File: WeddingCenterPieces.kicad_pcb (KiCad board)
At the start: 2 copper layers, 80 x 57 mm, 72 parts, among them J1 USB_C_Receptacle_USB2.0_16P, J2 DBG, J5 WS2812, K1 SW_Push, K2 SW_Push, K3 SW_Push, K4 SW_Push, SW1 Btn_OnBoard, SW2 RST, SW3 BOOT, U1 RP2040, U2 TPD2E2U06, U4 TXS0101DBV, U5 W25Q128JVSIQ, U6 TVS0500DRV, U7 AP2112K-3.3, U8 TXS0101DBV, Y1 12MHz

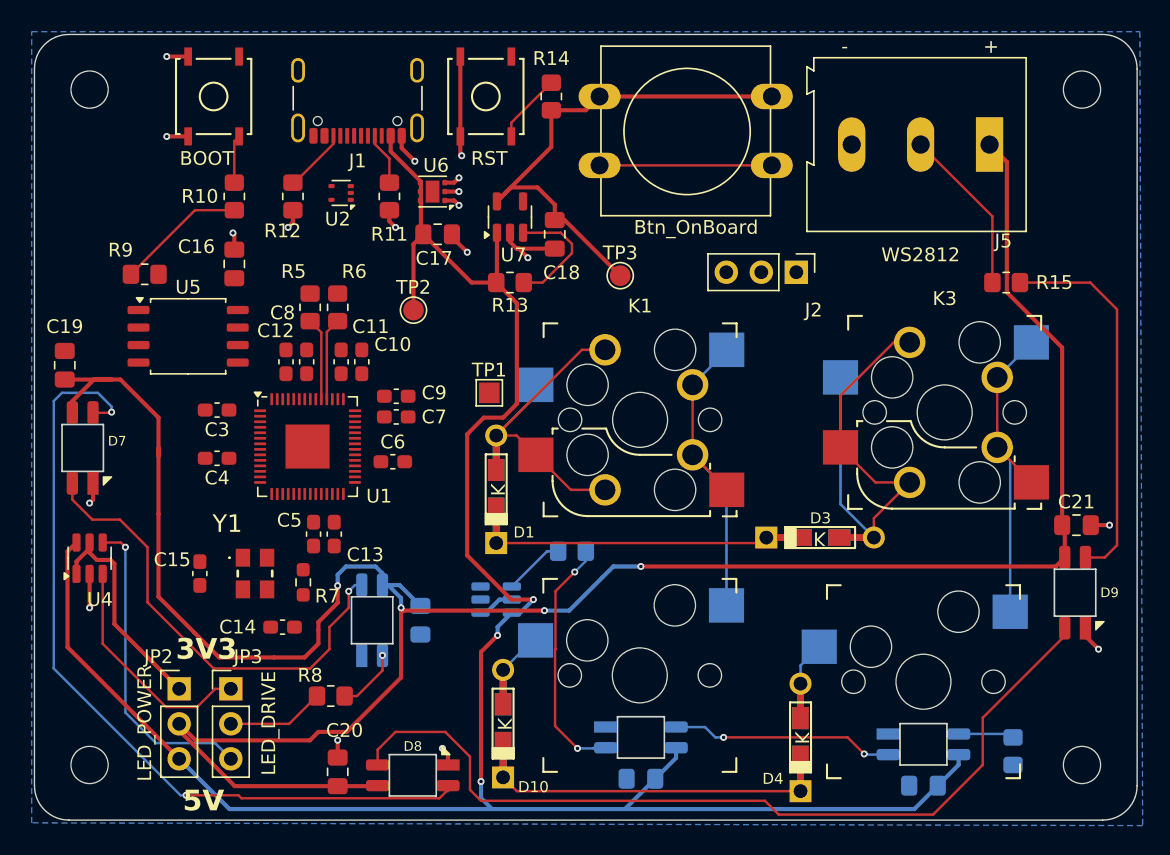
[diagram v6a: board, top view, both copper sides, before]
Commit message: Shrinking board to only have 2 key switches and a few other unnecessary components. Finished with routing the rest of the board.
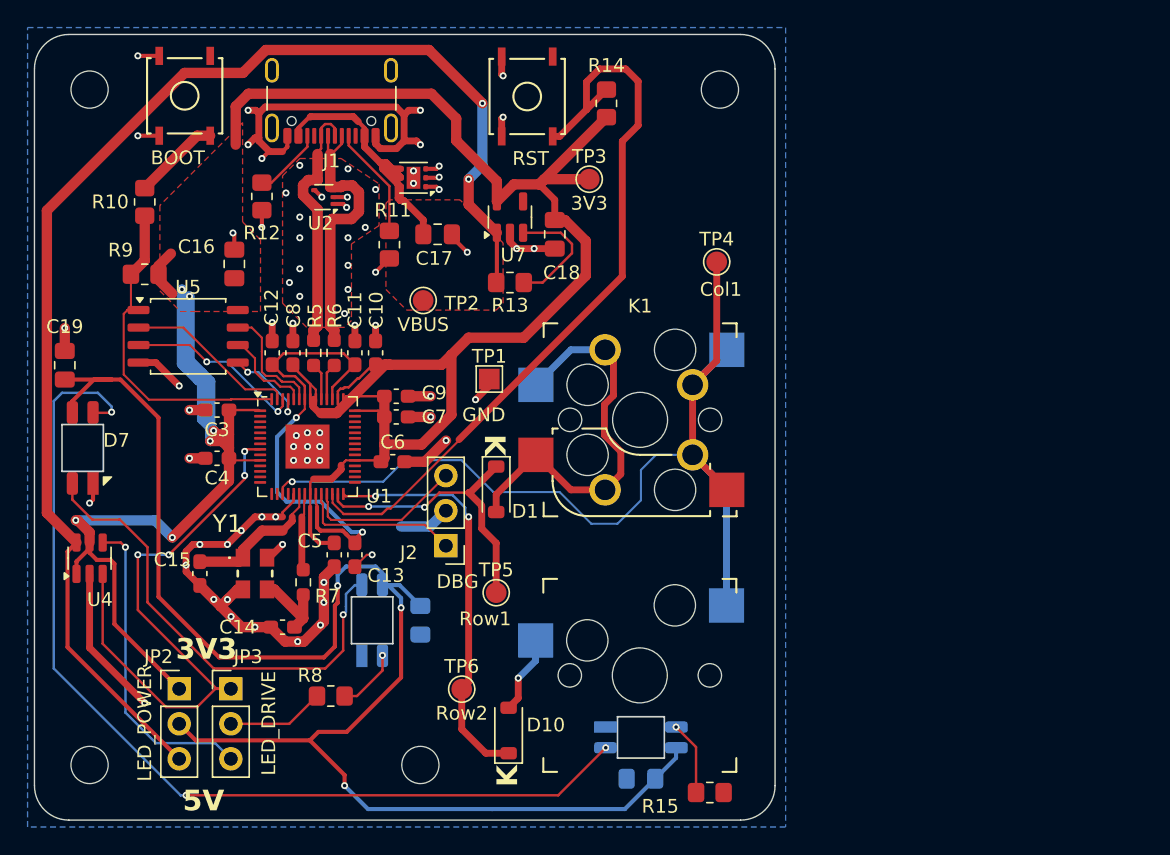
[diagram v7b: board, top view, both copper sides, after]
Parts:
- removed C20, C21, C23: 100nF, Capacitor_SMD:C_0805_2012Metric_Pad1.18x1.45mm_HandSolder
- removed D12, D8, D9: ~, Extra:SK6812-MINI-E_ReverseMount
- removed D3, D4: 1N4148W, Keebio-Parts:Diode-dual
- removed J5: WS2812, TerminalBlock:TerminalBlock_Altech_AK300-3_P5.00mm
- removed K3: SW_Push, keyswitches:Kailh_socket_MX_optional_reversible
- removed K4: SW_Push, keyswitches:Kailh_socket_MX
- removed R16, R17: 470, Resistor_SMD:R_0805_2012Metric_Pad1.20x1.40mm_HandSolder
- removed SW1: Btn_OnBoard, Button_Switch_THT:SW_PUSH-12mm
- removed U8: TXS0101DBV, Package_TO_SOT_SMD:SOT-23-6
- added TP4: Col1, TestPoint:TestPoint_Pad_D1.5mm, F.Cu at (135.5, 83.5)
- added TP5: Row1, TestPoint:TestPoint_Pad_D1.5mm, F.Cu at (119.5, 107.5)
- added TP6: Row2, TestPoint:TestPoint_Pad_D1.5mm, F.Cu at (117.0, 114.5)
- D1, D10: footprint Keebio-Parts:Diode-dual -> Diode_SMD:D_SOD-123
- R5, R6: footprint Resistor_SMD:R_0805_2012Metric_Pad1.20x1.40mm_HandSolder -> Resistor_SMD:R_0603_1608Metric_Pad0.98x0.95mm_HandSolder
- moved H4 48.0 mm to (114.0, 120.0)
- moved R15 42.8 mm to (135.0, 122.0), turned to 180 degrees
- moved J2 32.2 mm to (115.8, 104.1), turned to 180 degrees
- moved H2 26.3 mm to (135.7, 71.0)
- moved TP3 7.35 mm to (126.2, 77.5)
- moved R10 6.51 mm to (94.0, 79.2)
- moved R14 4.03 mm to (127.5, 72.0)
- moved R11 3.50 mm to (111.8, 82.2)
- moved R5 3.31 mm to (106.2, 90.1)
- moved R6 3.31 mm to (107.8, 90.1)
- moved SW2 3.00 mm to (121.8, 71.5)
- moved R12 2.25 mm to (102.5, 78.8)
- moved C13 2.12 mm to (109.2, 104.8)
- moved C5 2.12 mm to (107.8, 104.8)
- moved SW3 2.10 mm to (96.9, 71.5)
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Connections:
- C22 pad 1: VBUS -> /Lighting/PowerRail
- D11 pad 3: VBUS -> /Lighting/PowerRail
- D7 pad 4: Net-(D7-DOUT) -> Net-(D11-DIN)
- R15 pad 2: Net-(D9-DOUT) -> Net-(D11-DOUT)
- U1 pad 18: /Key Switches/COL_2 -> unconnected-(U1-GPIO15-Pad18)
- U1 pad 9: /Lighting/DIN_1 -> unconnected-(U1-GPIO7-Pad9)
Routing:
- net +3V3: track 56.6 -> 187.7 mm, vias 0 -> 6
- net GND: track 37.2 -> 122.6 mm, vias 18 -> 76
- net /Lighting/PowerRail: track 177.9 -> 111.3 mm, vias 4 -> 3
- net Net-(D8-DOUT): track 63.3 -> 0.00 mm
- net Net-(D7-DOUT): track 59.5 -> 0.00 mm, vias 2 -> 0
- net Net-(D11-DIN): track 18.0 -> 71.3 mm, vias 2 -> 3
- net Net-(U1-RUN): track 5.10 -> 55.6 mm
- net /Key Switches/COL_1: track 24.2 -> 70.1 mm, vias 0 -> 1
- net VBUS: track 156.0 -> 118.0 mm, vias 3 -> 2
- net /Microcontroller/+1.1V: track 0.00 -> 35.5 mm, vias 0 -> 2
- net Net-(D3-A): track 34.1 -> 0.00 mm
- net Net-(D9-DOUT): track 27.6 -> 0.00 mm
- net /Lighting/DIN_0: track 16.8 -> 43.2 mm, vias 0 -> 4
- net /Key Switches/COL_2: track 24.5 -> 0.00 mm
- net /External Connectors/D-: track 0.00 -> 20.4 mm
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- added copper zone on F.Cu, net +3V3
- added copper zone on F.Cu, net GND
- added copper zone on F.Cu, net VBUS
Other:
- board size 80 x 57 mm -> 53.7 x 57 mm
- board text added: "K"
- board text removed: "+"
- board text removed: "-"

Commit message: Outputs generated and prepared for ordering.
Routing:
- net /Key Switches/COL_1: track 70.1 -> 70.6 mm, vias 1 -> 2
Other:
- rule pad_to_mask_clearance: 0.0508 -> 0
- board text added: "v02 Wedding_Test Bare_RP2040 2024-12"
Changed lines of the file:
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@@
 			(dielectric_constraints no)
 		)
-		(pad_to_mask_clearance 0.0508)
+		(pad_to_mask_clearance 0)
 		(allow_soldermask_bridges_in_footprints no)
 		(pcbplotparams
@@
 			(plotinvisibletext no)
 			(sketchpadsonfab no)
-			(subtractmaskfromsilk no)
+			(subtractmaskfromsilk yes)
 			(outputformat 1)
 			(mirror no)
-			(drillshape 1)
+			(drillshape 0)
 			(scaleselection 1)
-			(outputdirectory "")
+			(outputdirectory "gerbers/")
 		)
 	)
@@
 		(tags "resistor handsolder")
 		(property "Reference" "R15"
-			(at 3.6 -1 0)
+			(at 3.8 -0.4 0)
 			(layer "F.SilkS")
 			(effects
@@
 		(layer "Edge.Cuts")
 	)
+	(gr_text "v02\nWedding_Test\nBare_RP2040\n2024-12"
+		(at 123.75 79.875 0)
+		(layer "B.Cu")
+		(effects
+			(font
+				(size 1.5 1.5)
+				(thickness 0.3)
+				(bold yes)
+			)
+			(justify right bottom mirror)
+		)
+	)
 	(gr_text "3V3"
 		(at 96.25 112.475 0)
@@
 	)
 	(via
-		(at 105.8 97.9)
+		(at 105.8 98.1)
 		(size 0.508)
 		(drill 0.254)
@@
 	)
 	(via
-		(at 105.8 95.9)
+		(at 105.8 95.7)
 		(size 0.508)
 		(drill 0.254)
@@
 	)
 	(via
-		(at 106.7 95.9)
+		(at 107 95.7)
 		(size 0.508)
 		(drill 0.254)
@@
 	)
 	(via
-		(at 104.8 96.9)
+		(at 104.7 96.9)
 		(size 0.508)
 		(drill 0.254)
@@
 	)
 	(via
-		(at 104.8 97.9)
+		(at 104.7 98.1)
 		(size 0.508)
 		(drill 0.254)
@@
 	)
 	(via
-		(at 106.7 97.9)
+		(at 107 98.1)
 		(size 0.508)
 		(drill 0.254)
@@
 	)
 	(via
-		(at 106.7 96.9)
+		(at 107 96.9)
 		(size 0.508)
 		(drill 0.254)
@@
 	)
 	(segment
-		(start 118.45 102.85)
-		(end 118.45 101.188943)
+		(start 119.5 107.5)
+		(end 119.5 103.9)
 		(width 0.5)
 		(layer "F.Cu")
@@
 	)
 	(segment
-		(start 119.5 107.5)
-		(end 119.5 103.9)
+		(start 119.5 103.9)
+		(end 118.45 102.85)
+		(width 0.5)
+		(layer "F.Cu")
+		(net 7)
+	)
+	(segment
+		(start 118.45 102.85)
+		(end 118.45 99.4)
 		(width 0.5)
 		(layer "F.Cu")
@@
 	)
 	(segment
-		(start 117.611057 100.238943)
-		(end 119.5 98.35)
-		(width 0.5)
+		(start 117.5 100.238943)
+		(end 117.611057 100.238943)
+		(width 0.18)
 		(layer "F.Cu")
 		(net 7)
 	)
 	(segment
-		(start 117.5 100.238943)
-		(end 117.611057 100.238943)
+		(start 118.45 99.4)
+		(end 119.5 98.35)
 		(width 0.5)
 		(layer "F.Cu")
@@
 	)
 	(segment
-		(start 119.5 103.9)
-		(end 118.45 102.85)
-		(width 0.5)
-		(layer "F.Cu")
-		(net 7)
-	)
-	(segment
-		(start 118.45 101.188943)
-		(end 117.5 100.238943)
-		(width 0.5)
+		(start 117.611057 100.238943)
+		(end 118.45 99.4)
+		(width 0.18)
 		(layer "F.Cu")
 		(net 7)
@@
 	)
 	(segment
+		(start 128.108521 88.163)
+		(end 132.365521 92.42)
+		(width 0.5)
+		(layer "F.Cu")
+		(net 31)
+	)
+	(segment
+		(start 126.737 88.163)
+		(end 128.108521 88.163)
+		(width 0.5)
+		(layer "F.Cu")
+		(net 31)
+	)
+	(segment
 		(start 136.23 100.04)
 		(end 136.23 99.98)
@@
 	)
 	(segment
+		(start 117.4 97.5)
+		(end 126.737 88.163)
+		(width 0.5)
+		(layer "F.Cu")
+		(net 31)
+	)
+	(segment
+		(start 132.365521 92.42)
+		(end 133.75 92.42)
+		(width 0.5)
+		(layer "F.Cu")
+		(net 31)
+	)
+	(segment
 		(start 135.5 90.67)
 		(end 135.5 83.5)
@@
 	)
 	(via
-		(at 104.697043 99.450052)
+		(at 117.4 97.5)
 		(size 0.508)
 		(drill 0.254)
@@
 		(net 31)
 	)
-	(segment
-		(start 130 100.8)
-		(end 130 98.6)
-		(width 0.1524)
-		(layer "B.Cu")
+	(via
+		(at 104.697043 99.450052)
+		(size 0.508)
+		(drill 0.254)
+		(layers "F.Cu" "B.Cu")
 		(net 31)
 	)
 	(segment
-		(start 128.3 102.5)
-		(end 130 100.8)
+		(start 116.9838 97.8838)
+		(end 117.0162 97.8838)
 		(width 0.1524)
 		(layer "B.Cu")
@@
 	)
 	(segment
-		(start 124.1 100.2)
-		(end 126.4 102.5)
-		(width 0.1524)
-		(layer "B.Cu")
-		(net 31)
-	)
-	(segment
-		(start 131.1 97.5)
-		(end 133.75 97.5)
-		(width 0.1524)
-		(layer "B.Cu")
-		(net 31)
-	)
-	(segment
 		(start 136.21 108.42)
 		(end 136.21 99.96)
@@
 	)
 	(segment
-		(start 130 98.6)
-		(end 131.1 97.5)
+		(start 117.0162 97.8838)
+		(end 117.4 97.5)
 		(width 0.1524)
 		(layer "B.Cu")
@@
 	)
 	(segment
-		(start 116.9838 97.8838)
-		(end 119.3 100.2)
-		(width 0.1524)
-		(layer "B.Cu")
-		(net 31)
-	)
-	(segment
 		(start 104.697043 99.450052)
 		(end 111.300131 99.450052)
@@
 		(layer "B.Cu")
 		(net 31)
-	)
-	(segment
-		(start 126.4 102.5)
-		(end 128.3 102.5)
-		(width 0.1524)
-		(layer "B.Cu")
-		(net 31)
-	)
-	(segment
-		(start 119.3 100.2)
-		(end 124.1 100.2)
-		(width 0.1524)
-		(layer "B.Cu")
-		(net 31)
